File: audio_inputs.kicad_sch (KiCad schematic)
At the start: 10 parts, among them J2 PLR237/T10BK, U5 DIR9001PW

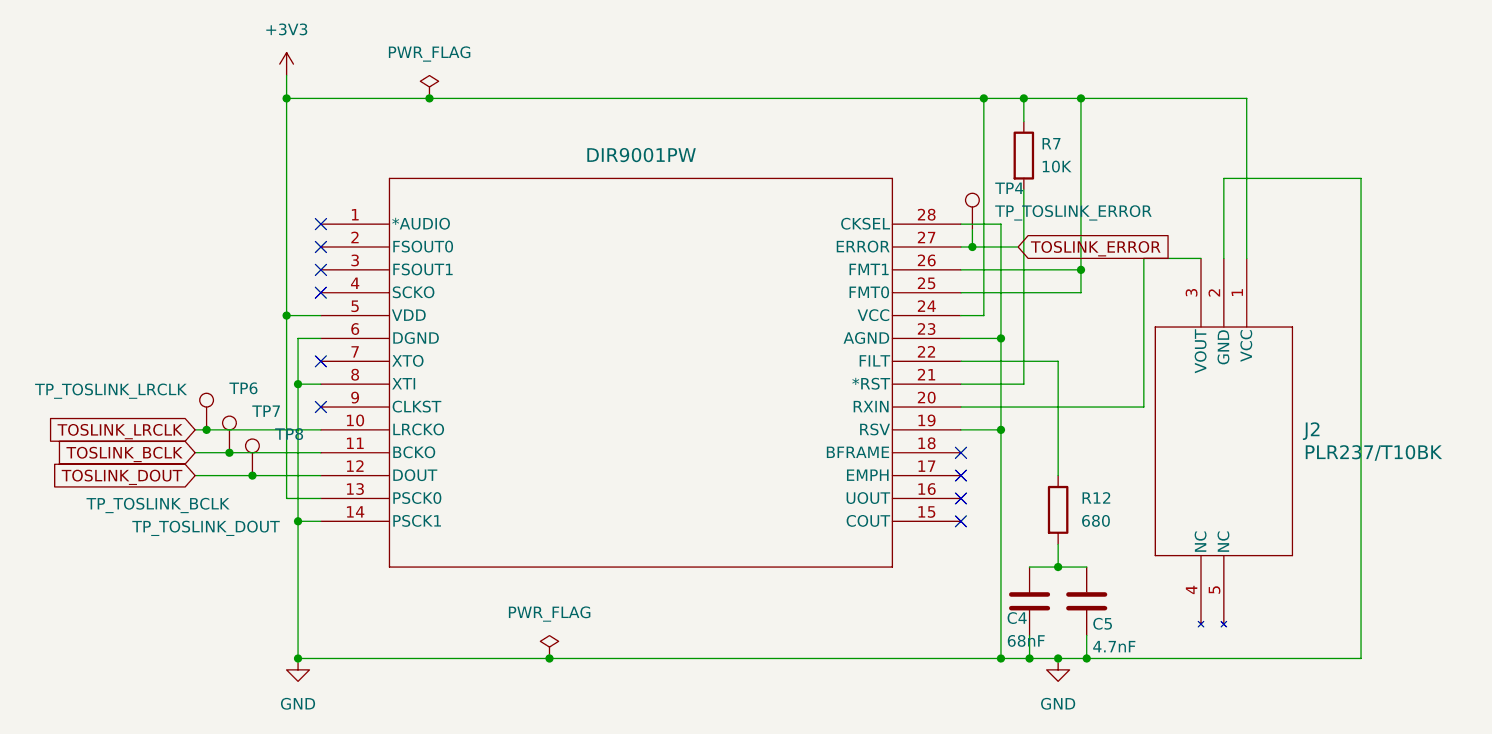
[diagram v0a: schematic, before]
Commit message: Fixed dotstar positioning.  Minor changes to PCB
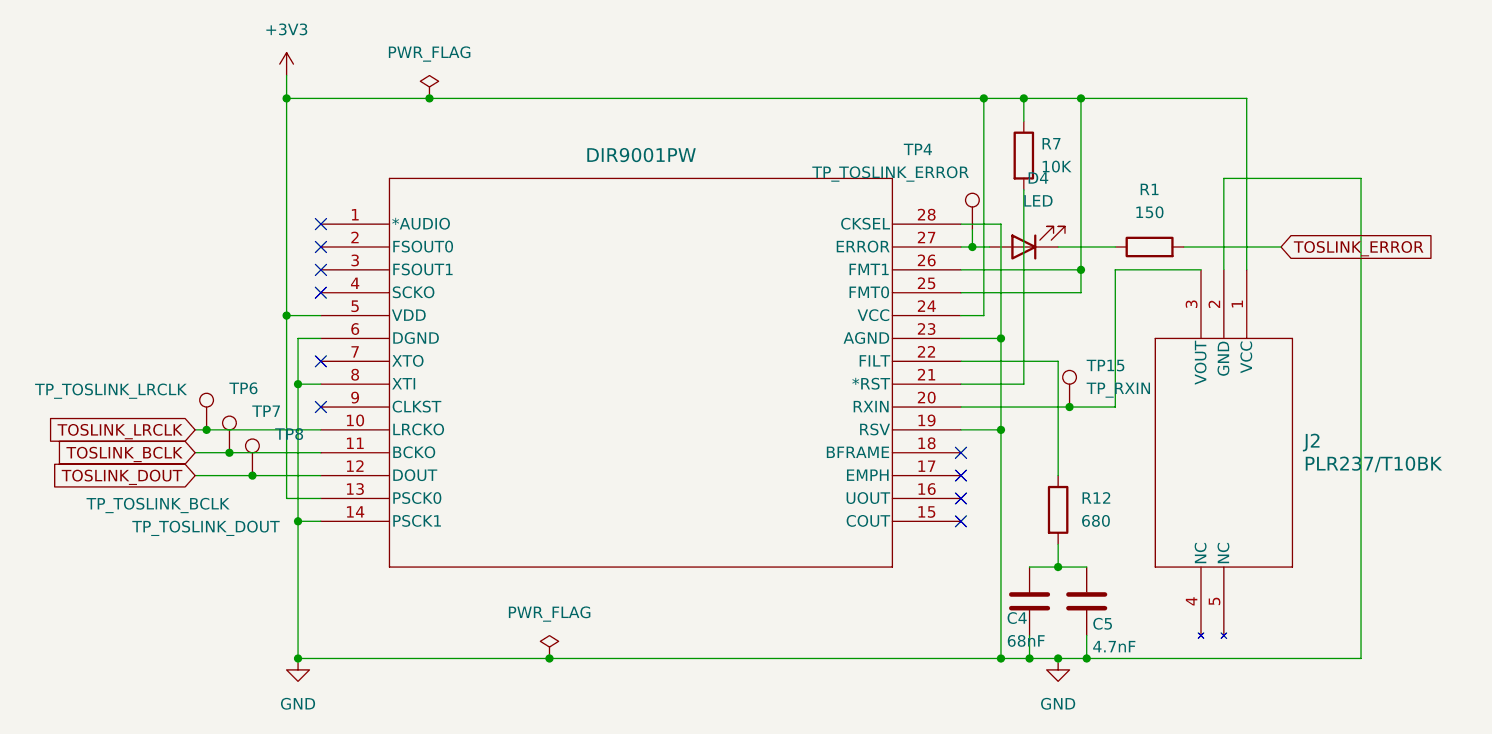
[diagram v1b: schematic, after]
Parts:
- added D4: LED, LED_SMD:LED_0805_2012Metric_Pad1.15x1.40mm_HandSolder, symbol Device:LED
- added R1: 150, Resistor_SMD:R_0805_2012Metric_Pad1.20x1.40mm_HandSolder, symbol Device:R
- added TP15: TP_RXIN, TestPoint:TestPoint_Pad_D1.0mm, symbol Connector:TestPoint
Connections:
- net TOSLINK_ERROR: now also R1.2; no longer TP4.1, U5.27 (ERROR)
- net at J2.3 (VOUT), U5.20 (RXIN): now also TP15.1
- new net: D4.2 (A), TP4.1, U5.27 (ERROR)
- new net: D4.1 (K), R1.1
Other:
- moved on the sheet: J2

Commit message: Final changes before ordering.
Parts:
- D4: value LED -> NCD0805R1; LCSC (none) -> C17471
- J2, TP15, TP4, TP6, TP7, TP8: DNP (none) -> 1; now left out of the parts list
- R1: LCSC (none) -> C17471
- R7: value 10K -> 10k
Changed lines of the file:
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@@
 		(unit 1)
 		(exclude_from_sim no)
-		(in_bom yes)
+		(in_bom no)
 		(on_board yes)
 		(dnp no)
@@
 			)
 		)
+		(property "DNP" "1"
+			(at 150.495 115.57 0)
+			(effects
+				(font
+					(size 1.27 1.27)
+				)
+				(hide yes)
+			)
+		)
 		(pin "1"
 		)
@@
 		(unit 1)
 		(exclude_from_sim no)
-		(in_bom yes)
+		(in_bom no)
 		(on_board yes)
 		(dnp no)
@@
 		)
 		(property "Description" "test point"
+			(at 54.61 118.11 0)
+			(effects
+				(font
+					(size 1.27 1.27)
+				)
+				(hide yes)
+			)
+		)
+		(property "DNP" "1"
 			(at 54.61 118.11 0)
 			(effects
@@
 			)
 		)
-		(property "Value" "LED"
+		(property "Value" "NCD0805R1"
 			(at 147.0025 92.71 0)
 			(effects
@@
 			)
 		)
+		(property "LCSC" "C17471"
+			(at 145.415 97.79 0)
+			(effects
+				(font
+					(size 1.27 1.27)
+				)
+				(hide yes)
+			)
+		)
 		(pin "1"
 		)
@@
 		(unit 1)
 		(exclude_from_sim no)
-		(in_bom yes)
+		(in_bom no)
 		(on_board yes)
 		(dnp no)
@@
 			)
 		)
+		(property "DNP" "1"
+			(at 170.18 100.33 90)
+			(effects
+				(font
+					(size 1.27 1.27)
+				)
+				(hide yes)
+			)
+		)
 		(pin "1"
 		)
@@
 		(unit 1)
 		(exclude_from_sim no)
-		(in_bom yes)
+		(in_bom no)
 		(on_board yes)
 		(dnp no)
@@
 		)
 		(property "Description" "test point"
+			(at 57.15 120.65 0)
+			(effects
+				(font
+					(size 1.27 1.27)
+				)
+				(hide yes)
+			)
+		)
+		(property "DNP" "1"
 			(at 57.15 120.65 0)
 			(effects
@@
 			)
 		)
-		(property "Value" "10K"
+		(property "Value" "10k"
 			(at 147.32 88.8999 0)
 			(effects
@@
 		(unit 1)
 		(exclude_from_sim no)
-		(in_bom yes)
+		(in_bom no)
 		(on_board yes)
 		(dnp no)
@@
 		)
 		(property "Description" "test point"
+			(at 59.7037 123.19 0)
+			(effects
+				(font
+					(size 1.27 1.27)
+				)
+				(hide yes)
+			)
+		)
+		(property "DNP" "1"
 			(at 59.7037 123.19 0)
 			(effects
@@
 		(unit 1)
 		(exclude_from_sim no)
-		(in_bom yes)
+		(in_bom no)
 		(on_board yes)
 		(dnp no)
@@
 		)
 		(property "Description" "test point"
+			(at 139.7 95.885 0)
+			(effects
+				(font
+					(size 1.27 1.27)
+				)
+				(hide yes)
+			)
+		)
+		(property "DNP" "1"
 			(at 139.7 95.885 0)
 			(effects
@@
 			(effects
 				(font
+					(size 1.27 1.27)
+				)
+				(hide yes)
+			)
+		)
+		(property "LCSC" "C17471"
+			(at 159.385 97.79 90)
+			(effects
+				(font

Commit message: Cleaned up a lot around the PCM1862.  ADC side looking pretty good
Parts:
- D4: footprint LED_SMD:LED_0805_2012Metric_Pad1.15x1.40mm_HandSolder -> (none); LCSC C17471 -> C2994781
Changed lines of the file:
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@@
 			)
 		)
-		(property "Footprint" "LED_SMD:LED_0805_2012Metric_Pad1.15x1.40mm_HandSolder"
+		(property "Footprint" ""
 			(at 145.415 97.79 0)
 			(effects
@@
 			)
 		)
-		(property "LCSC" "C17471"
+		(property "LCSC" "C2994781"
 			(at 145.415 97.79 0)
 			(effects

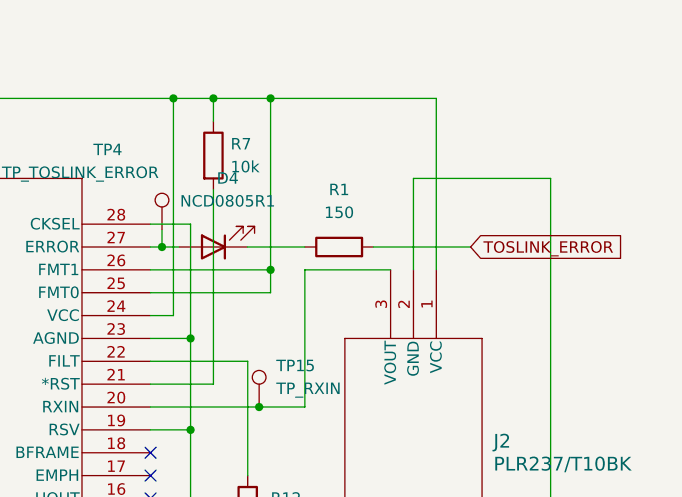
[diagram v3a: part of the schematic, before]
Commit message: Removed 3v3 rail going across the board.  Rotated dotstars to put pin 1 upper left.
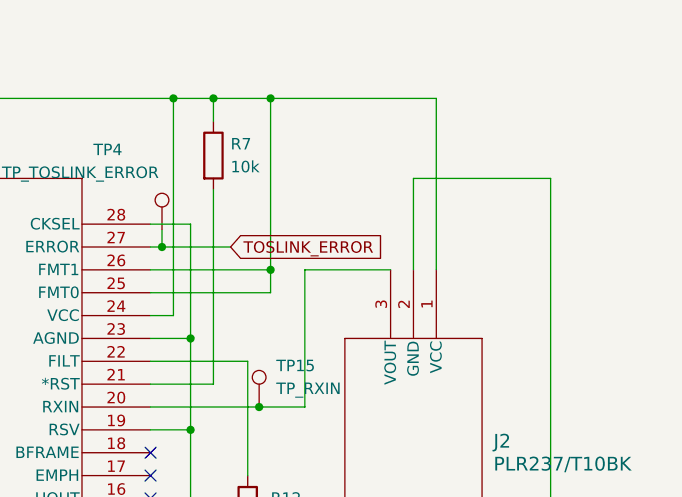
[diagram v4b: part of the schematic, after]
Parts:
- removed D4: NCD0805R1, symbol Device:LED
- removed R1: 150, Resistor_SMD:R_0805_2012Metric_Pad1.20x1.40mm_HandSolder, symbol Device:R
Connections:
- net TOSLINK_ERROR: now also TP4.1, U5.27 (ERROR)
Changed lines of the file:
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@@
-	(wire
-		(pts
-			(xy 163.195 97.79) (xy 173.99 97.79)
-		)
-		(stroke
-			(width 0)
-			(type default)
-		)
-	)
 	(wire
 		(pts
@@
 	(wire
 		(pts
-			(xy 149.225 97.79) (xy 155.575 97.79)
-		)
-		(stroke
-			(width 0)
-			(type default)
-		)
-	)
-	(wire
-		(pts
 			(xy 64.77 143.51) (xy 92.71 143.51)
 		)
@@
 	(wire
 		(pts
-			(xy 139.7 97.79) (xy 141.605 97.79)
+			(xy 139.7 97.79) (xy 147.32 97.79)
 		)
 		(stroke
@@
 	(global_label "TOSLINK_ERROR"
 		(shape input)
-		(at 173.99 97.79 0)
+		(at 147.32 97.79 0)
 		(fields_autoplaced yes)
 		(effects
@@
 		)
 		(property "Intersheetrefs" "${INTERSHEET_REFS}"
-			(at 192.0684 97.79 0)
+			(at 165.3984 97.79 0)
 			(effects
 				(font
@@
 	)
 	(symbol
-		(lib_id "Device:LED")
-		(at 145.415 97.79 180)
-		(unit 1)
-		(exclude_from_sim no)
-		(in_bom yes)
-		(on_board yes)
-		(dnp no)
-		(fields_autoplaced yes)
-		(property "Reference" "D4"
-			(at 147.0025 90.17 0)
-			(effects
-				(font
-					(size 1.27 1.27)
-				)
-			)
-		)
-		(property "Value" "NCD0805R1"
-			(at 147.0025 92.71 0)
-			(effects
-				(font
-					(size 1.27 1.27)
-				)
-			)
-		)
-		(property "Footprint" ""
-			(at 145.415 97.79 0)
-			(effects
-				(font
-					(size 1.27 1.27)
-				)
-				(hide yes)
-			)
-		)
-		(property "Datasheet" "~"
-			(at 145.415 97.79 0)
-			(effects
-				(font
-					(size 1.27 1.27)
-				)
-				(hide yes)
-			)
-		)
-		(property "Description" "Light emitting diode"
-			(at 145.415 97.79 0)
-			(effects
-				(font
-					(size 1.27 1.27)
-				)
-				(hide yes)
-			)
-		)
-		(property "Sim.Pins" "1=K 2=A"
-			(at 145.415 97.79 0)
-			(effects
-				(font
-					(size 1.27 1.27)
-				)
-				(hide yes)
-			)
-		)
-		(property "LCSC" "C2994781"
-			(at 145.415 97.79 0)
-			(effects
-				(font
-					(size 1.27 1.27)
-				)
-				(hide yes)
-			)
-		)
-		(pin "1"
-		)
-		(pin "2"
-		)
-		(instances
-			(project ""
-				(path "/e63e39d7-6ac0-4ffd-8aa3-1841a4541b55/69671d55-966b-4bba-8a79-dc8715674913"
-					(reference "D4")
-					(unit 1)
-				)
-			)
-		)
-	)
-	(symbol
 		(lib_id "PLR237/T10BK:PLR237_T10BK")
 		(at 170.18 100.33 270)
@@
 					(unit 1)
 				)
-			)
-		)
-	)
-	(symbol
-		(lib_id "Device:R")
-		(at 159.385 97.79 90)
-		(unit 1)
-		(exclude_from_sim no)
-		(in_bom yes)
-		(on_board yes)
-		(dnp no)
-		(fields_autoplaced yes)
-		(property "Reference" "R1"
-			(at 159.385 91.44 90)
-			(effects
-				(font
-					(size 1.27 1.27)
-				)
-			)
-		)
-		(property "Value" "150"
-			(at 159.385 93.98 90)
-			(effects
-				(font
-					(size 1.27 1.27)
-				)
-			)
-		)
-		(property "Footprint" "Resistor_SMD:R_0805_2012Metric_Pad1.20x1.40mm_HandSolder"
-			(at 159.385 99.568 90)
-			(effects
-				(font
-					(size 1.27 1.27)
-				)
-				(hide yes)
-			)
-		)
-		(property "Datasheet" "~"
-			(at 159.385 97.79 0)
-			(effects
-				(font
-					(size 1.27 1.27)
-				)
-				(hide yes)
-			)
-		)
-		(property "Description" "Resistor"
-			(at 159.385 97.79 0)
-			(effects
-				(font
-					(size 1.27 1.27)
-				)
-				(hide yes)
-			)
-		)
-		(property "LCSC" "C17471"
-			(at 159.385 97.79 90)
-			(effects
-				(font
-					(size 1.27 1.27)
-				)
-				(hide yes)
-			)
-		)
-		(pin "2"
-		)
-		(pin "1"
-		)
-		(instances
-			(project ""
-				(path "/e63e39d7-6ac0-4ffd-8aa3-1841a4541b55/69671d55-966b-4bba-8a79-dc8715674913"
-					(reference "R1")
-					(unit 1)
-				)

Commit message: Final changes for production run
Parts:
- added D4: LED_RED, LED_SMD:LED_0402_1005Metric, symbol Device:LED
- added D5: LED_GREEN, LED_SMD:LED_0402_1005Metric, symbol Device:LED
- added R16, R17: 330, Resistor_SMD:R_0402_1005Metric, symbol Device:R
- C4, C5: footprint Capacitor_SMD:C_0805_2012Metric_Pad1.18x1.45mm_HandSolder -> Capacitor_SMD:C_0805_2012Metric
- R12: footprint Resistor_SMD:R_0805_2012Metric_Pad1.20x1.40mm_HandSolder -> Resistor_SMD:R_0402_1005Metric
- R7: footprint Resistor_SMD:R_0805_2012Metric_Pad1.20x1.40mm_HandSolder -> Resistor_SMD:R_0805_2012Metric
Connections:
- net +3V3: now also R16.1
- net GND: now also D5.1 (K)
- net TOSLINK_ERROR: now also D4.1 (K)
- net GPIO23_OPT_LOCK: now reaches U5.9 (CLKST)
- net GPIO23_OPT_LOCK: now also R17.1
- new net: D5.2 (A), R17.2
- new net: D4.2 (A), R16.2
- no-connect marks 10 -> 9
